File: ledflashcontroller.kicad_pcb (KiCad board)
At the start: 2 copper layers, 100 x 100 mm, 68 parts, among them J1 Conn_02x08_Odd_Even, J2 CONN_01X02, J3 CONN_01X02, K1 LDD-1000H, K2 LDD-1000H, P1 V_IN, P10 BNC, P11 BNC, P12 BNC, P2 I2C_HEADER, P3 GPIO_HEADER, P4 V_DIM1, P5 V_DIM2, P6 V_OUT, P7 BNC, P8 BNC, P9 BNC, Q1 IRLML6244, Q2 IRFB3256, U1 Teensy3.6, U10 DMC2700, U2 ISO1540, U3 DMC2700, U4 DMC2700, U5 ISO1540, U6 DMC2700, U7 DMC2700, U8 ISO1540, U9 DMC2700

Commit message: Completed Ratsnest
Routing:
- net /SDA: track 7.01 -> 86.1 mm, vias 0 -> 3
- net +5V: track 182.2 -> 210.9 mm, vias 15 -> 17
- net /DIM1: track 46.3 -> 34.2 mm
- net Net-(R12-Pad2): track 13.3 -> 20.0 mm, vias 1 -> 2
- net GND: track 728.4 -> 731.8 mm, vias 19 -> 21
- net /TrigInOutPu3/TRIG_CON1: track 26.5 -> 29.0 mm
- net /TrigInOutPu2/TRIG_CON1: track 26.5 -> 29.0 mm
- net /TrigInOutPu1/TRIG_CON1: track 26.5 -> 29.0 mm
- net /SW2: track 31.5 -> 29.1 mm
- net +3V3: track 190.0 -> 191.1 mm

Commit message: Refinement
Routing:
- net +3V3: track 191.1 -> 178.9 mm
- net Net-(R12-Pad2): track 20.0 -> 13.3 mm, vias 2 -> 1
- net /SDA: track 86.1 -> 90.3 mm
- net /TRIG_IO9: track 64.8 -> 67.2 mm
- net /TRIG_IO8: track 57.3 -> 59.4 mm
- net GND: track 731.8 -> 730.2 mm
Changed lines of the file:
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@@
   (general
     (links 203)
-    (no_connects 0)
+    (no_connects 1)
     (area 29.924999 29.924999 130.075001 130.075001)
     (thickness 1.6)
@@
     (last_trace_width 0.4)
     (trace_clearance 0.2)
-    (zone_clearance 0.508)
+    (zone_clearance 1)
     (zone_45_only yes)
     (trace_min 0.2)
@@
   (segment (start 44 108.95) (end 44 111) (width 0.4) (layer F.Cu) (net 1))
   (via (at 44 111) (size 0.6) (drill 0.4) (layers F.Cu B.Cu) (net 1))
+  (segment (start 106.3115 92) (end 106.3115 91.575736) (width 0.5) (layer B.Cu) (net 2))
+  (segment (start 106.611499 92.299999) (end 106.3115 92) (width 0.5) (layer F.Cu) (net 2))
+  (segment (start 107.3115 93) (end 106.611499 92.299999) (width 0.5) (layer F.Cu) (net 2))
+  (segment (start 108 93) (end 107.3115 93) (width 0.5) (layer F.Cu) (net 2))
+  (via (at 106.3115 82.5) (size 0.6) (drill 0.4) (layers F.Cu B.Cu) (net 2))
+  (segment (start 106.3115 91.575736) (end 106.3115 82.5) (width 0.5) (layer B.Cu) (net 2))
+  (segment (start 105.5 82.5) (end 106.3115 82.5) (width 0.5) (layer F.Cu) (net 2))
+  (via (at 106.3115 92) (size 0.6) (drill 0.4) (layers F.Cu B.Cu) (net 2))
   (segment (start 98.9 54.25) (end 100 54.25) (width 0.5) (layer F.Cu) (net 2))
   (segment (start 100 54.25) (end 101 54.25) (width 0.5) (layer F.Cu) (net 2))
@@
   (segment (start 42 70) (end 42 73) (width 0.5) (layer B.Cu) (net 2))
   (via (at 42 73) (size 0.6) (drill 0.4) (layers F.Cu B.Cu) (net 2))
-  (segment (start 43 70) (end 42 70) (width 0.5) (layer F.Cu) (net 2))
   (segment (start 42 70) (end 37.12 70) (width 0.5) (layer F.Cu) (net 2))
   (segment (start 42 55.205) (end 42 70) (width 0.5) (layer B.Cu) (net 2))
@@
   (segment (start 104.54 93) (end 108 93) (width 0.5) (layer F.Cu) (net 2))
   (segment (start 108 93) (end 117 93) (width 0.5) (layer F.Cu) (net 2))
-  (segment (start 108 92) (end 108 93) (width 0.5) (layer F.Cu) (net 2))
-  (segment (start 108 82.5) (end 108 92) (width 0.5) (layer B.Cu) (net 2))
-  (via (at 108 92) (size 0.6) (drill 0.4) (layers F.Cu B.Cu) (net 2))
-  (segment (start 105.5 82.5) (end 108 82.5) (width 0.5) (layer F.Cu) (net 2))
-  (via (at 108 82.5) (size 0.6) (drill 0.4) (layers F.Cu B.Cu) (net 2))
   (segment (start 109.295 105.3) (end 110.095 105.3) (width 0.5) (layer F.Cu) (net 2))
   (segment (start 105.5 82.5) (end 105.5 92.04) (width 0.5) (layer B.Cu) (net 2))
@@
   (segment (start 89.5 47.4908) (end 89.5 32.2) (width 1) (layer F.Cu) (net 8))
   (segment (start 66.86 69.62) (end 69.4 69.62) (width 1) (layer F.Cu) (net 8))
+  (segment (start 102 85) (end 118 85) (width 0.4) (layer F.Cu) (net 9))
   (segment (start 68.44 96.24) (end 71.2 99) (width 0.4) (layer F.Cu) (net 9))
   (segment (start 83.85 100.7) (end 84 100.7) (width 0.4) (layer F.Cu) (net 9))
@@
   (segment (start 117 100.7) (end 119.33 98.37) (width 0.4) (layer F.Cu) (net 9))
   (segment (start 119.33 98.37) (end 119.33 93.33) (width 0.4) (layer F.Cu) (net 9))
-  (segment (start 118 85) (end 109.4 85) (width 0.4) (layer F.Cu) (net 9))
   (segment (start 119 93) (end 118 92) (width 0.4) (layer B.Cu) (net 9))
   (segment (start 118 92) (end 118 85) (width 0.4) (layer B.Cu) (net 9))
@@
   (segment (start 125 75.75) (end 118.5 75.75) (width 0.4) (layer F.Cu) (net 9))
   (segment (start 118.5 75.75) (end 118 76.25) (width 0.4) (layer F.Cu) (net 9))
-  (segment (start 102 85) (end 109.4 85) (width 0.4) (layer F.Cu) (net 9))
-  (segment (start 109.4 85) (end 118 76.4) (width 0.4) (layer F.Cu) (net 9))
   (segment (start 118 76.4) (end 118 76.25) (width 0.4) (layer F.Cu) (net 9))
   (segment (start 102 85) (end 96.67 85) (width 0.4) (layer F.Cu) (net 9))
@@
   (segment (start 125 79.75) (end 125 87.54) (width 0.4) (layer F.Cu) (net 10))
   (segment (start 125 87.54) (end 121.75 90.79) (width 0.4) (layer F.Cu) (net 10))
+  (segment (start 118 80.25) (end 111.875112 80.25) (width 0.4) (layer F.Cu) (net 11))
+  (segment (start 111.875112 80.25) (end 108.125112 84) (width 0.4) (layer F.Cu) (net 11))
+  (segment (start 108.125112 85.736152) (end 108.125112 84) (width 0.4) (layer B.Cu) (net 11))
+  (via (at 108.125112 84) (size 0.6) (drill 0.4) (layers F.Cu B.Cu) (net 11))
+  (segment (start 53.880001 83.880001) (end 97.670001 83.880001) (width 0.4) (layer F.Cu) (net 11))
+  (segment (start 97.670001 83.880001) (end 98.050002 83.5) (width 0.4) (layer F.Cu) (net 11))
+  (segment (start 98.050002 83.5) (end 103.070002 83.5) (width 0.4) (layer F.Cu) (net 11))
+  (segment (start 53.5 83.5) (end 53.880001 83.880001) (width 0.4) (layer F.Cu) (net 11))
+  (segment (start 103.070002 83.5) (end 103.5 83.929998) (width 0.4) (layer F.Cu) (net 11))
+  (segment (start 103.5 83.929998) (end 108.05511 83.929998) (width 0.4) (layer F.Cu) (net 11))
+  (segment (start 108.05511 83.929998) (end 108.125112 84) (width 0.4) (layer F.Cu) (net 11))
+  (segment (start 108.549376 85.736152) (end 108.125112 85.736152) (width 0.4) (layer F.Cu) (net 11))
+  (segment (start 118.29985 85.736152) (end 108.549376 85.736152) (width 0.4) (layer F.Cu) (net 11))
+  (segment (start 118.700001 85.336001) (end 118.29985 85.736152) (width 0.4) (layer F.Cu) (net 11))
+  (via (at 108.125112 85.736152) (size 0.6) (drill 0.4) (layers F.Cu B.Cu) (net 11))
   (segment (start 121.75 85.71) (end 120.547919 85.71) (width 0.4) (layer F.Cu) (net 11))
   (segment (start 120.547919 85.71) (end 120.17392 85.336001) (width 0.4) (layer F.Cu) (net 11))
@@
   (segment (start 118 81.65) (end 118.700001 82.350001) (width 0.4) (layer F.Cu) (net 11))
   (segment (start 118.700001 82.350001) (end 118.700001 85.336001) (width 0.4) (layer F.Cu) (net 11))
-  (segment (start 118.700001 85.336001) (end 116.536002 87.5) (width 0.4) (layer F.Cu) (net 11))
-  (segment (start 116.536002 87.5) (end 111 87.5) (width 0.4) (layer F.Cu) (net 11))
-  (segment (start 111 80.5) (end 111 87.5) (width 0.4) (layer B.Cu) (net 11))
-  (via (at 111 87.5) (size 0.6) (drill 0.4) (layers F.Cu B.Cu) (net 11))
-  (segment (start 53.5 83.5) (end 53.880001 83.880001) (width 0.4) (layer F.Cu) (net 11))
-  (segment (start 53.880001 83.880001) (end 97.670001 83.880001) (width 0.4) (layer F.Cu) (net 11))
-  (segment (start 97.670001 83.880001) (end 98.050002 83.5) (width 0.4) (layer F.Cu) (net 11))
-  (segment (start 98.050002 83.5) (end 104.079998 83.5) (width 0.4) (layer F.Cu) (net 11))
-  (segment (start 104.079998 83.5) (end 104.329999 83.750001) (width 0.4) (layer F.Cu) (net 11))
-  (segment (start 104.329999 83.750001) (end 107.749999 83.750001) (width 0.4) (layer F.Cu) (net 11))
-  (segment (start 107.749999 83.750001) (end 111 80.5) (width 0.4) (layer F.Cu) (net 11))
-  (via (at 111 80.5) (size 0.6) (drill 0.4) (layers F.Cu B.Cu) (net 11))
   (segment (start 53.2 81) (end 53.2 83.2) (width 0.4) (layer B.Cu) (net 11))
   (segment (start 53.2 83.2) (end 53.5 83.5) (width 0.4) (layer B.Cu) (net 11))
@@
   (segment (start 76.06 92.06) (end 76 92) (width 0.4) (layer B.Cu) (net 30))
   (via (at 76 92) (size 0.6) (drill 0.4) (layers F.Cu B.Cu) (net 30))
+  (segment (start 107.01151 79.48849) (end 109.5 77) (width 0.4) (layer B.Cu) (net 31))
+  (segment (start 110.5 102.5) (end 107.01151 99.01151) (width 0.4) (layer B.Cu) (net 31))
+  (segment (start 107.01151 99.01151) (end 107.01151 79.48849) (width 0.4) (layer B.Cu) (net 31))
   (segment (start 86.5 77) (end 86.5 80.72) (width 0.4) (layer B.Cu) (net 31))
   (segment (start 86.5 80.72) (end 86.22 81) (width 0.4) (layer B.Cu) (net 31))
   (segment (start 109.5 77) (end 86.5 77) (width 0.4) (layer F.Cu) (net 31))
   (via (at 86.5 77) (size 0.6) (drill 0.4) (layers F.Cu B.Cu) (net 31))
-  (segment (start 109.5 101.5) (end 109.5 77) (width 0.4) (layer B.Cu) (net 31))
   (via (at 109.5 77) (size 0.6) (drill 0.4) (layers F.Cu B.Cu) (net 31))
-  (segment (start 110.5 102.5) (end 109.5 101.5) (width 0.4) (layer B.Cu) (net 31))
   (segment (start 111.9 102.8) (end 110.8 102.8) (width 0.4) (layer F.Cu) (net 31))
   (segment (start 110.8 102.8) (end 110.5 102.5) (width 0.4) (layer F.Cu) (net 31))
@@
   (segment (start 78.6 91.1) (end 78.5 91) (width 0.4) (layer B.Cu) (net 32))
   (via (at 78.5 91) (size 0.6) (drill 0.4) (layers F.Cu B.Cu) (net 32))
+  (segment (start 112.5 100.5) (end 109.17122 97.17122) (width 0.4) (layer B.Cu) (net 33))
+  (segment (start 109.17122 97.17122) (end 109.17122 78.82878) (width 0.4) (layer B.Cu) (net 33))
+  (segment (start 109.17122 78.82878) (end 112 76) (width 0.4) (layer B.Cu) (net 33))
   (segment (start 84 76.5) (end 83.68 76.82) (width 0.4) (layer B.Cu) (net 33))
   (segment (start 83.68 76.82) (end 83.68 81) (width 0.4) (layer B.Cu) (net 33))
@@
   (segment (start 84.5 76) (end 84 76.5) (width 0.4) (layer F.Cu) (net 33))
   (via (at 84 76.5) (size 0.6) (drill 0.4) (layers F.Cu B.Cu) (net 33))
-  (segment (start 112.5 100.5) (end 112.5 76.5) (width 0.4) (layer B.Cu) (net 33))
-  (segment (start 112.5 76.5) (end 112 76) (width 0.4) (layer B.Cu) (net 33))
   (via (at 112 76) (size 0.6) (drill 0.4) (layers F.Cu B.Cu) (net 33))
   (segment (start 84 80.68) (end 83.68 81) (width 0.4) (layer B.Cu) (net 33))
@@
   (segment (start 123.6 60.9) (end 123.6 47.5) (width 0.4) (layer F.Cu) (net 49))
   (segment (start 119 61) (end 123.5 61) (width 0.4) (layer F.Cu) (net 49))
-  (segment (start 126 107) (end 126.15 107) (width 0.4) (layer F.Cu) (net 50))
-  (via (at 127.5 113) (size 0.6) (drill 0.4) (layers F.Cu B.Cu) (net 50))
-  (segment (start 126.15 107) (end 127.5 108.35) (width 0.4) (layer F.Cu) (net 50))
-  (segment (start 127.5 109.151458) (end 127.5 113) (width 0.4) (layer F.Cu) (net 50))
-  (segment (start 127.5 108.35) (end 127.5 109.151458) (width 0.4) (layer F.Cu) (net 50))
   (segment (start 123 113) (end 123.9 113) (width 0.4) (layer F.Cu) (net 50))
   (segment (start 123.9 113) (end 124.2 113.3) (width 0.4) (layer F.Cu) (net 50))

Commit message: Refinement2
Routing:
- net +3V3: track 178.9 -> 190.9 mm, vias 4 -> 5
- net Net-(K2-Pad11): track 50.7 -> 50.8 mm, vias 1 -> 0
- net Net-(R12-Pad2): vias 1 -> 2
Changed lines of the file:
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@@
   (general
     (links 203)
-    (no_connects 1)
+    (no_connects 0)
     (area 29.924999 29.924999 130.075001 130.075001)
     (thickness 1.6)
     (drawings 8)
-    (tracks 946)
+    (tracks 952)
     (zones 0)
     (modules 68)
@@
   (segment (start 74.8 44.595) (end 74.8 32.2092) (width 1) (layer F.Cu) (net 4))
   (segment (start 62 69.74) (end 59.46 69.74) (width 1) (layer F.Cu) (net 4))
-  (segment (start 65 47.5) (end 65 51.5) (width 1) (layer B.Cu) (net 5))
-  (segment (start 65 51.5) (end 62 54.5) (width 1) (layer B.Cu) (net 5))
+  (segment (start 62 54.5) (end 62 50.5) (width 1) (layer F.Cu) (net 5))
+  (segment (start 62 50.5) (end 65 47.5) (width 1) (layer F.Cu) (net 5))
   (segment (start 65 47.5) (end 65 32.2092) (width 1) (layer F.Cu) (net 5))
   (segment (start 59.46 54.5) (end 62 54.5) (width 1) (layer F.Cu) (net 5))
@@
   (segment (start 66 75) (end 89.5 75) (width 0.4) (layer F.Cu) (net 6))
   (via (at 89.5 75) (size 0.6) (drill 0.4) (layers F.Cu B.Cu) (net 6))
-  (segment (start 88.5 54.5) (end 69.52 54.5) (width 1) (layer F.Cu) (net 7))
+  (segment (start 69.4 54.38) (end 88.400802 54.38) (width 1) (layer F.Cu) (net 7))
+  (segment (start 96.395 47.4908) (end 99.3 47.4908) (width 1) (layer F.Cu) (net 7))
+  (segment (start 88.400802 54.38) (end 95.290002 47.4908) (width 1) (layer F.Cu) (net 7))
+  (segment (start 95.290002 47.4908) (end 96.395 47.4908) (width 1) (layer F.Cu) (net 7))
   (segment (start 69.52 54.5) (end 69.4 54.38) (width 1) (layer F.Cu) (net 7))
-  (segment (start 99.3 47.4908) (end 95.5092 47.4908) (width 1) (layer B.Cu) (net 7))
-  (segment (start 95.5092 47.4908) (end 88.5 54.5) (width 1) (layer B.Cu) (net 7))
-  (via (at 88.5 54.5) (size 0.6) (drill 0.4) (layers F.Cu B.Cu) (net 7))
   (segment (start 99.3 47.4908) (end 99.3 44.5858) (width 1) (layer F.Cu) (net 7))
   (segment (start 99.3 44.5858) (end 99.3 32.2) (width 1) (layer F.Cu) (net 7))
@@
   (segment (start 89.5 47.4908) (end 89.5 32.2) (width 1) (layer F.Cu) (net 8))
   (segment (start 66.86 69.62) (end 69.4 69.62) (width 1) (layer F.Cu) (net 8))
+  (segment (start 116 76) (end 117.75 76) (width 0.4) (layer F.Cu) (net 9))
+  (segment (start 117.75 76) (end 118 76.25) (width 0.4) (layer F.Cu) (net 9))
+  (segment (start 118 85) (end 118 78) (width 0.4) (layer B.Cu) (net 9))
+  (segment (start 118 78) (end 116 76) (width 0.4) (layer B.Cu) (net 9))
+  (via (at 116 76) (size 0.6) (drill 0.4) (layers F.Cu B.Cu) (net 9))
   (segment (start 102 85) (end 118 85) (width 0.4) (layer F.Cu) (net 9))
   (segment (start 68.44 96.24) (end 71.2 99) (width 0.4) (layer F.Cu) (net 9))
@@
   (segment (start 123.6 60.9) (end 123.6 47.5) (width 0.4) (layer F.Cu) (net 49))
   (segment (start 119 61) (end 123.5 61) (width 0.4) (layer F.Cu) (net 49))
+  (via (at 127.5 113) (size 0.6) (drill 0.4) (layers F.Cu B.Cu) (net 50))
   (segment (start 123 113) (end 123.9 113) (width 0.4) (layer F.Cu) (net 50))
   (segment (start 123.9 113) (end 124.2 113.3) (width 0.4) (layer F.Cu) (net 50))

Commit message: RTC update
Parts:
- added C7: 100n, Capacitors_SMD:C_0603, F.Cu at (159.9, 58.5)
- added C8: 1u, Capacitors_SMD:C_0603, F.Cu at (159.4, 74.1)
- added J4: Conn_01x02, Pin_Headers:Pin_Header_Straight_1x02_Pitch2.54mm, F.Cu at (162.5, 88.5)
- added U11: DS3231, Housings_SOIC:SOIC-16W_7.5x10.3mm_Pitch1.27mm, F.Cu at (146.2, 89.3)
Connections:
- U1 pad 36: (no net) -> /RTC_SQW
- U1 pad 43: (no net) -> /RTC_RST
- U1 pad 44: (no net) -> /RTC_32kHz

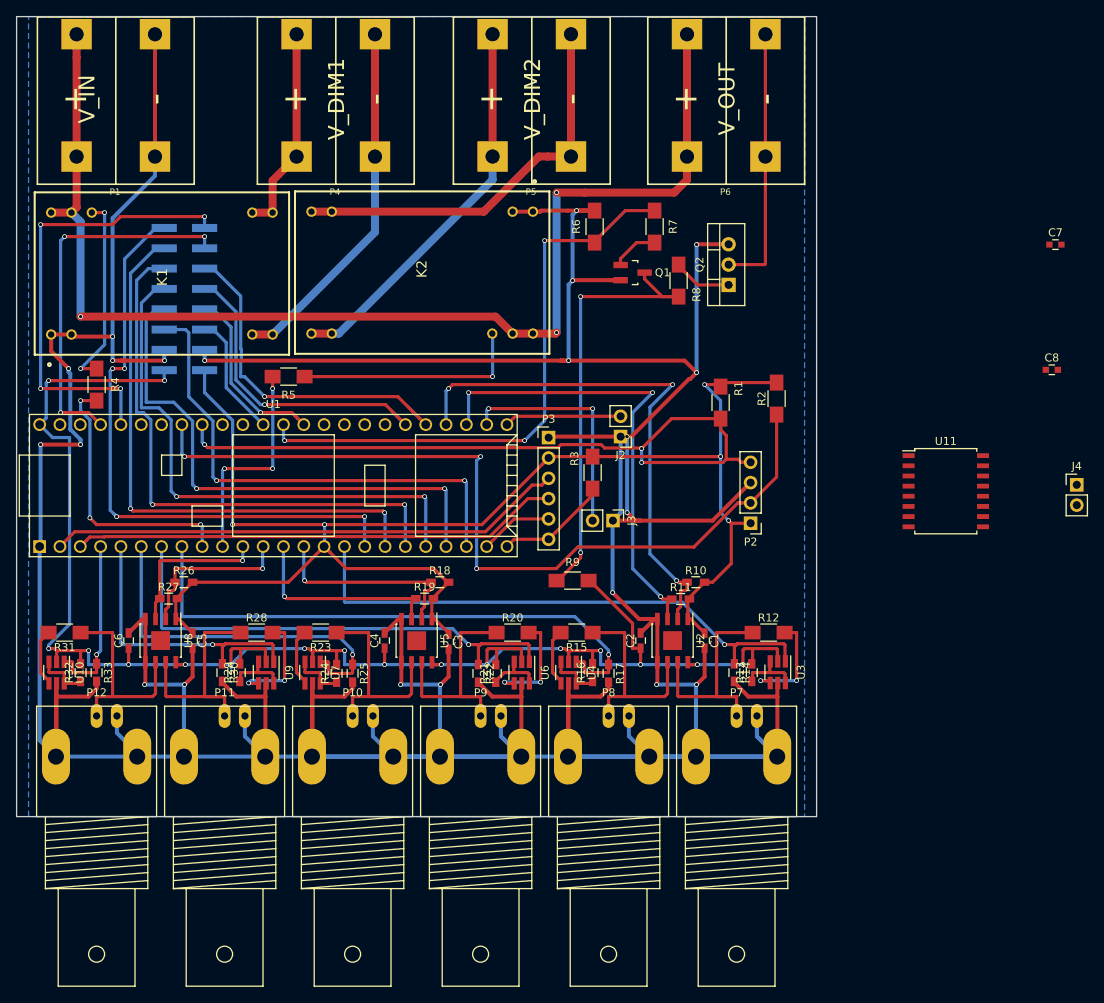
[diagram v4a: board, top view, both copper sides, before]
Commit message: Connected RTC and git tried to get rid of vias
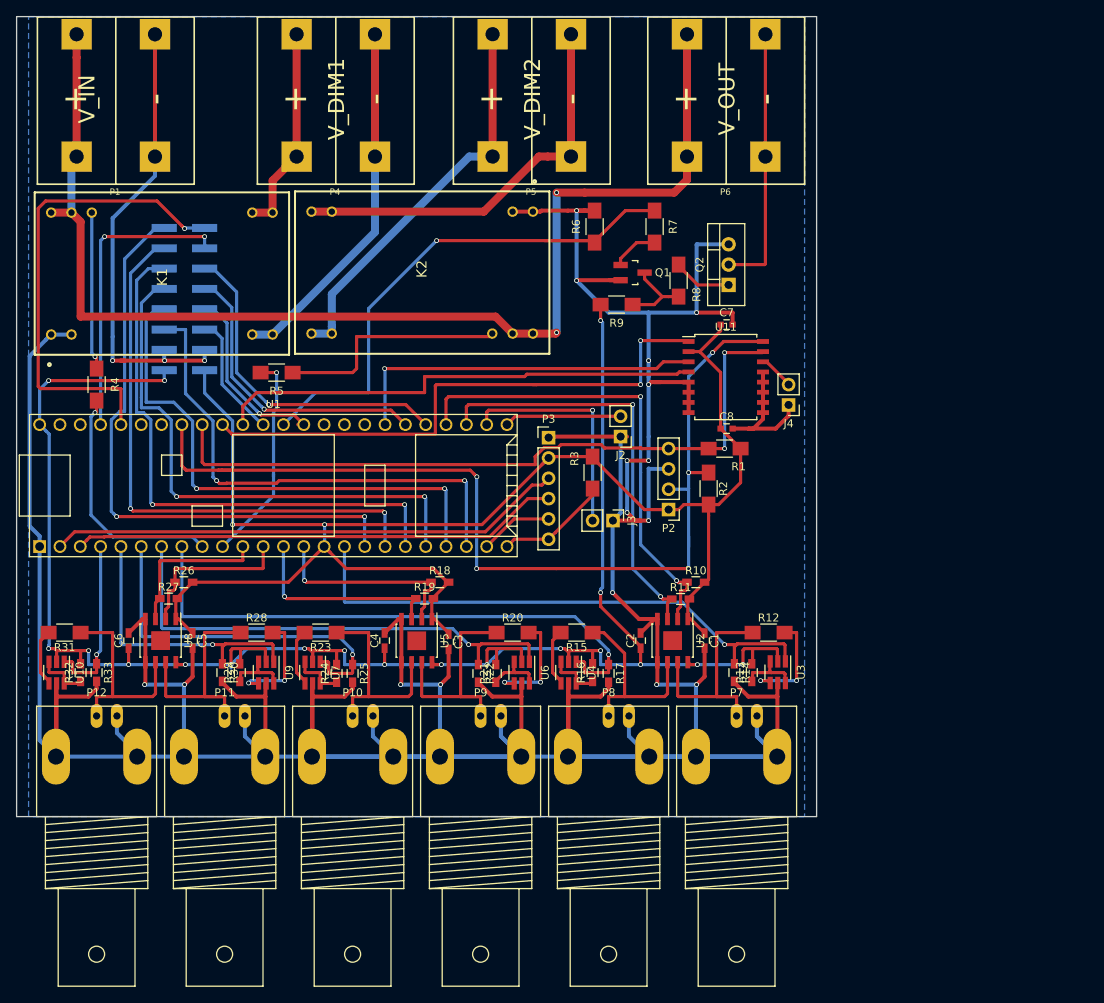
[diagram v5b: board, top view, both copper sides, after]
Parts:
- moved C7 42.3 mm to (118.8, 68.5)
- moved C8 41.3 mm to (118.8, 81.5)
- moved J4 37.4 mm to (126.5, 78.5), turned to 180 degrees
- moved R9 34.9 mm to (105.0, 66.0), turned to 180 degrees
- moved U11 31.0 mm to (118.7, 75.1)
- moved R2 14.1 mm to (116.5, 89.0), turned to 270 degrees
- moved P2 10.4 mm to (111.5, 91.6)
- moved R1 5.77 mm to (118.5, 84.0), turned to 0 degrees
- moved R5 1.58 mm to (62.5, 74.5)
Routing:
- net /RTC_32kHz: track 0.00 -> 70.9 mm, vias 0 -> 2
- net /RTC_RST: track 0.00 -> 61.2 mm
- net /RTC_SQW: track 0.00 -> 45.5 mm, vias 0 -> 1
- net Net-(Q1-Pad3): track 55.2 -> 10.2 mm, vias 2 -> 0
- net GND: track 730.2 -> 693.8 mm, vias 21 -> 19
- net +5V: track 210.9 -> 240.9 mm, vias 17 -> 19
- net /SCL: track 105.4 -> 124.8 mm, vias 3 -> 5
- net /TRIG_IO2: track 46.8 -> 37.7 mm, vias 3 -> 2
- net /TRIG_IO9: track 67.2 -> 59.8 mm, vias 3 -> 2
- net /TRIG_IO8: track 59.4 -> 53.3 mm, vias 3 -> 2
- net Net-(K1-Pad22): track 24.3 -> 19.8 mm, vias 2 -> 1
- net /RTC_VBAT: track 0.00 -> 4.44 mm
- net /DIM1: track 34.2 -> 30.2 mm, vias 3 -> 1
- net /VOUT: track 73.7 -> 69.9 mm, vias 3 -> 1
- net /TRIG_IO10: track 45.1 -> 41.6 mm
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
